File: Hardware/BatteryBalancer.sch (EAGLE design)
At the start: 91 parts, among them IC1 OP-AMP, J2 ISP, Q1 MOSFET_PCH-IRLML2244, U1 TAP_POINT, U10 MCP1755, U11 AD7280A, U12 ATMEGA328P_TQFP, U13 CH340C, U2 TAP_POINT, U3 TAP_POINT, U4 TAP_POINT, U5 TAP_POINT, U6 SINGLECELL, U7 SINGLECELL, U8 SINGLECELL, U9 SINGLECELL, Y1 16MHz

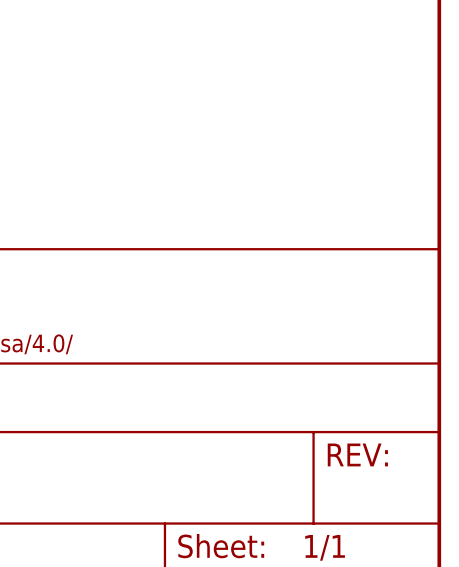
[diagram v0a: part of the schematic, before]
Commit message: Increase manufacturability, re panelize + CAM
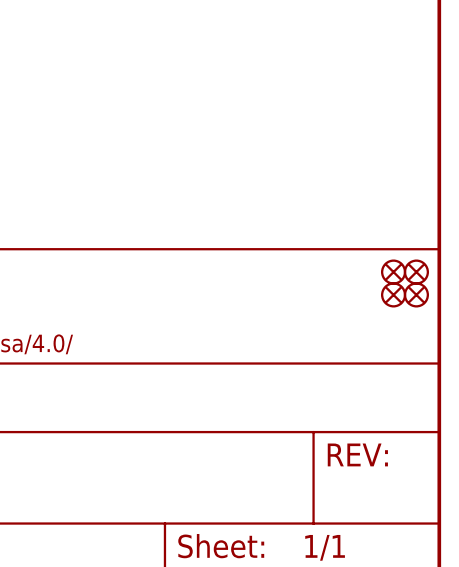
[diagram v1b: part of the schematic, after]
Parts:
- added FD1, FD2, FD3, FD4: FIDUCIALUFIDUCIAL, SparkFun-Aesthetics:FIDUCIALUFIDUCIAL
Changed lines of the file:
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@@
 <layer number="115" name="ReferenceISLANDS" color="7" fill="1" visible="yes" active="yes"/>
 <layer number="116" name="Patch_BOT" color="9" fill="4" visible="yes" active="yes"/>
+<layer number="117" name="PM_Ref" color="26" fill="1" visible="yes" active="yes"/>
 <layer number="118" name="Rect_Pads" color="7" fill="1" visible="yes" active="yes"/>
+<layer number="119" name="PF_Ref" color="31" fill="1" visible="yes" active="yes"/>
+<layer number="120" name="WFL_Ref" color="25" fill="1" visible="yes" active="yes"/>
 <layer number="121" name="_tsilk" color="7" fill="1" visible="yes" active="yes"/>
 <layer number="122" name="_bsilk" color="7" fill="1" visible="yes" active="yes"/>
@@
 <part name="R10" library="SparkFun-Resistors" deviceset="330KOHM" device="-0603-1/10W-1%" value="330k"/>
 <part name="R34" library="SparkFun-Resistors" deviceset="10MOHM" device="-0603-1/10W-5%" value="10M"/>
+<part name="FD1" library="SparkFun-Aesthetics" deviceset="FIDUCIAL" device="UFIDUCIAL"/>
+<part name="FD2" library="SparkFun-Aesthetics" deviceset="FIDUCIAL" device="UFIDUCIAL"/>
+<part name="FD3" library="SparkFun-Aesthetics" deviceset="FIDUCIAL" device="UFIDUCIAL"/>
+<part name="FD4" library="SparkFun-Aesthetics" deviceset="FIDUCIAL" device="UFIDUCIAL"/>
 </parts>
 <sheets>
@@
 </instance>
 <instance part="R34" gate="G$1" x="50.8" y="215.9" rot="R90"/>
+<instance part="FD1" gate="G$1" x="429.26" y="33.02"/>
+<instance part="FD2" gate="G$1" x="426.72" y="33.02"/>
+<instance part="FD3" gate="G$1" x="426.72" y="30.48"/>
+<instance part="FD4" gate="G$1" x="429.26" y="30.48"/>
 </instances>
 <busses>
